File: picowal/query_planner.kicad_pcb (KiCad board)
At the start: 4 copper layers, 100 x 55 mm, 23 parts, among them J1 UP, J2 DN, J3 UART, J4 SWD_QRY, J5 RJ45, J6 SWD_IDX, U1 iCE40HX8K, U10 AP2112K_1V2, U11 RP2354B_IDX, U12 PSRAM_IDX, U13 W5500, U14 W25Q128_IDX, U15 TPS62A01_IDX, U2 RP2354B_QRY, U3 SRAM_A, U4 SRAM_B, U5 PSRAM_QRY, U6 W25Q128_QRY, U7 W25Q32, U8 TPS62A01_QRY, U9 AP2112K_3V3, Y1 12MHz, Y2 25MHz

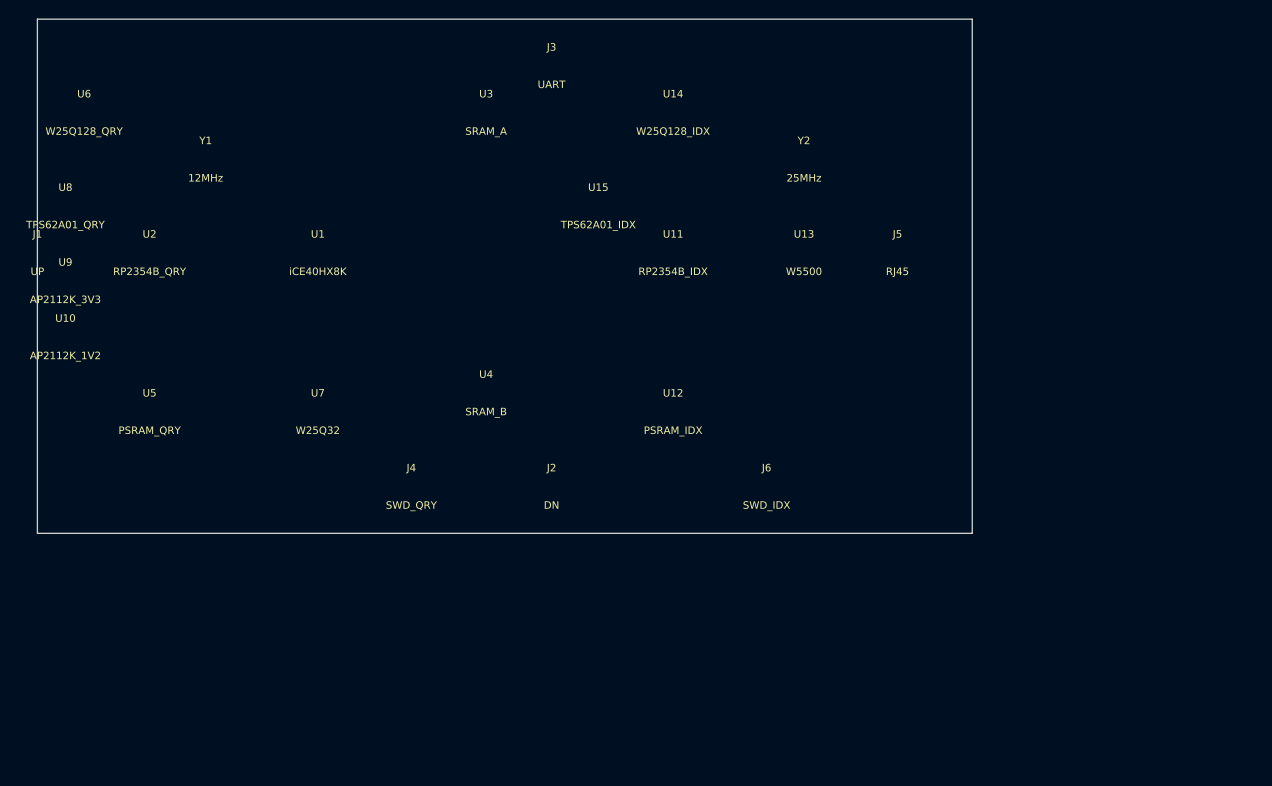
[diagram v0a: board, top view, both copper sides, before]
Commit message: Upgrade PicoWAL: iCE40HX8K → ECP5-5G-45F + 3× NVMe M.2 RAID
Swap FPGA to LFE5UM5G-45F (CABGA381) for 4× 3.125Gbps SerDes.
3 SerDes channels → PCIe Gen1 x1 → M.2 M-key NVMe drives (RAID).
4th SerDes spare for future upstream PCIe or inter-card link.

New components:
  - 3× M.2 M-key NVMe connectors (J7/J8/J9)
  - 100MHz LVDS differential oscillator (PCIe refclk)
  - TPS54331 3A buck for NVMe 3.3V power rail
  - TPS62A02 buck for ECP5 1.1V core (replaces AP2112K-1.2 LDO)
  - W25Q128 replaces W25Q32 for ECP5 config (45F bitstream is larger)

Board: 100×55mm → 130×80mm to accommodate M.2 slots.
BOM: £31.90 → £48.60 (excl. NVMe SSDs).
Pin budget: 110/205 I/O + 3/4 SerDes channels used.
Power: 2.8W board logic + ~10W for 3× NVMe drives.
RTL tests: 15/15 PASS (comment-only changes in query_bypass.v).

Co-authored-by: Copilot <223556219+Copilot@users.noreply.github.com>
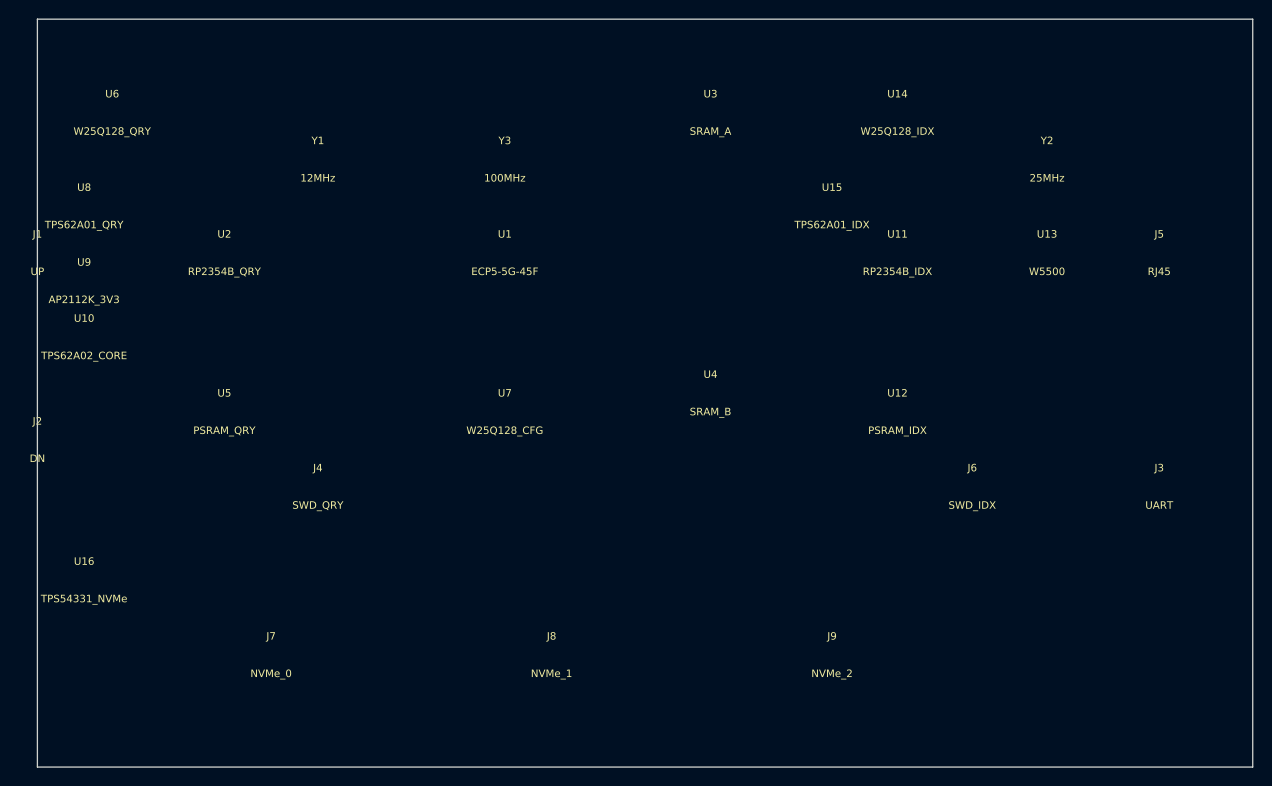
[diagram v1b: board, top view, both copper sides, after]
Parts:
- added J7: NVMe_0, Connector_M2:M2_M_Key_22x80, F.Cu at (25.0, 68.0)
- added J8: NVMe_1, Connector_M2:M2_M_Key_22x80, F.Cu at (55.0, 68.0)
- added J9: NVMe_2, Connector_M2:M2_M_Key_22x80, F.Cu at (85.0, 68.0)
- added U16: TPS54331_NVMe, Package_SO:SOIC-8_3.9x4.9mm_P1.27mm, F.Cu at (5.00, 60.0)
- added Y3: 100MHz, Oscillator:Oscillator_SMD_3225-4Pin_3.2x2.5mm, F.Cu at (50.0, 15.0)
- U1: value iCE40HX8K -> ECP5-5G-45F; footprint Package_BGA:BGA-256_14x14mm_P0.8mm -> Package_BGA:BGA-381_17x17mm_P0.8mm
- U10: value AP2112K_1V2 -> TPS62A02_CORE; footprint Package_TO_SOT_SMD:SOT-23-5 -> Package_TO_SOT_SMD:SOT-23-6
- U7: value W25Q32 -> W25Q128_CFG
- moved J3 79.1 mm to (120.0, 50.0)
- moved J2 55.2 mm to (0.00, 45.0)
- moved J5 28.0 mm to (120.0, 25.0)
- moved U13 26.0 mm to (108.0, 25.0)
- moved Y2 26.0 mm to (108.0, 15.0)
- moved U15 25.0 mm to (85.0, 20.0)
- moved U11 24.0 mm to (92.0, 25.0)
- moved U12 24.0 mm to (92.0, 42.0)
- moved U14 24.0 mm to (92.0, 10.0)
- moved U3 24.0 mm to (72.0, 10.0)
- moved U4 24.0 mm to (72.0, 40.0)
- moved J6 22.0 mm to (100.0, 50.0)
- moved U1 20.0 mm to (50.0, 25.0)
- moved U7 20.0 mm to (50.0, 42.0)
- moved Y1 12.0 mm to (30.0, 15.0)
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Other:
- board size 100 x 55 mm -> 130 x 80 mm
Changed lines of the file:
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@@
   (setup (grid_origin 0 0)
     (pcbplotparams (layerselection 0x00010fc_ffffffff) (outputdirectory "")))
-  (gr_rect (start 0 0) (end 100 55)
+  (gr_rect (start 0 0) (end 130 80)
     (stroke (width 0.1) (type default)) (fill none) (layer "Edge.Cuts"))
-  (footprint "Package_BGA:BGA-256_14x14mm_P0.8mm"
-    (at 30 25) (layer "F.Cu")
+  (footprint "Package_BGA:BGA-381_17x17mm_P0.8mm"
+    (at 50 25) (layer "F.Cu")
     (property "Reference" "U1" (at 0 -2 0) (layer "F.SilkS")
       (effects (font (size 0.8 0.8) (thickness 0.12))))
-    (property "Value" "iCE40HX8K" (at 0 2 0) (layer "F.SilkS")
+    (property "Value" "ECP5-5G-45F" (at 0 2 0) (layer "F.SilkS")
       (effects (font (size 0.8 0.8) (thickness 0.12)))))
   (footprint "Package_DFN_QFN:QFN-80-1EP_10x10mm_P0.4mm_EP5.45x5.45mm"
-    (at 12 25) (layer "F.Cu")
+    (at 20 25) (layer "F.Cu")
     (property "Reference" "U2" (at 0 -2 0) (layer "F.SilkS")
       (effects (font (size 0.8 0.8) (thickness 0.12))))
@@
       (effects (font (size 0.8 0.8) (thickness 0.12)))))
   (footprint "Package_SO:TSOP-II-44_10.16x18.41mm_P0.8mm"
-    (at 48 10) (layer "F.Cu")
+    (at 72 10) (layer "F.Cu")
     (property "Reference" "U3" (at 0 -2 0) (layer "F.SilkS")
       (effects (font (size 0.8 0.8) (thickness 0.12))))
@@
       (effects (font (size 0.8 0.8) (thickness 0.12)))))
   (footprint "Package_SO:TSOP-II-44_10.16x18.41mm_P0.8mm"
-    (at 48 40) (layer "F.Cu")
+    (at 72 40) (layer "F.Cu")
     (property "Reference" "U4" (at 0 -2 0) (layer "F.SilkS")
       (effects (font (size 0.8 0.8) (thickness 0.12))))
@@
       (effects (font (size 0.8 0.8) (thickness 0.12)))))
   (footprint "Package_SO:SOP-8_3.9x4.9mm_P1.27mm"
-    (at 12 42) (layer "F.Cu")
+    (at 20 42) (layer "F.Cu")
     (property "Reference" "U5" (at 0 -2 0) (layer "F.SilkS")
       (effects (font (size 0.8 0.8) (thickness 0.12))))
@@
       (effects (font (size 0.8 0.8) (thickness 0.12)))))
   (footprint "Package_SO:SOIC-8_3.9x4.9mm_P1.27mm"
-    (at 5 10) (layer "F.Cu")
+    (at 8 10) (layer "F.Cu")
     (property "Reference" "U6" (at 0 -2 0) (layer "F.SilkS")
       (effects (font (size 0.8 0.8) (thickness 0.12))))
@@
       (effects (font (size 0.8 0.8) (thickness 0.12)))))
   (footprint "Package_SO:SOIC-8_3.9x4.9mm_P1.27mm"
-    (at 30 42) (layer "F.Cu")
+    (at 50 42) (layer "F.Cu")
     (property "Reference" "U7" (at 0 -2 0) (layer "F.SilkS")
       (effects (font (size 0.8 0.8) (thickness 0.12))))
-    (property "Value" "W25Q32" (at 0 2 0) (layer "F.SilkS")
+    (property "Value" "W25Q128_CFG" (at 0 2 0) (layer "F.SilkS")
       (effects (font (size 0.8 0.8) (thickness 0.12)))))
   (footprint "Package_TO_SOT_SMD:SOT-23-6"
-    (at 3 20) (layer "F.Cu")
+    (at 5 20) (layer "F.Cu")
     (property "Reference" "U8" (at 0 -2 0) (layer "F.SilkS")
       (effects (font (size 0.8 0.8) (thickness 0.12))))
@@
       (effects (font (size 0.8 0.8) (thickness 0.12)))))
   (footprint "Package_TO_SOT_SMD:SOT-23-5"
-    (at 3 28) (layer "F.Cu")
+    (at 5 28) (layer "F.Cu")
     (property "Reference" "U9" (at 0 -2 0) (layer "F.SilkS")
       (effects (font (size 0.8 0.8) (thickness 0.12))))
     (property "Value" "AP2112K_3V3" (at 0 2 0) (layer "F.SilkS")
       (effects (font (size 0.8 0.8) (thickness 0.12)))))
-  (footprint "Package_TO_SOT_SMD:SOT-23-5"
-    (at 3 34) (layer "F.Cu")
+  (footprint "Package_TO_SOT_SMD:SOT-23-6"
+    (at 5 34) (layer "F.Cu")
     (property "Reference" "U10" (at 0 -2 0) (layer "F.SilkS")
       (effects (font (size 0.8 0.8) (thickness 0.12))))
-    (property "Value" "AP2112K_1V2" (at 0 2 0) (layer "F.SilkS")
+    (property "Value" "TPS62A02_CORE" (at 0 2 0) (layer "F.SilkS")
       (effects (font (size 0.8 0.8) (thickness 0.12)))))
   (footprint "Package_DFN_QFN:QFN-80-1EP_10x10mm_P0.4mm_EP5.45x5.45mm"
-    (at 68 25) (layer "F.Cu")
+    (at 92 25) (layer "F.Cu")
     (property "Reference" "U11" (at 0 -2 0) (layer "F.SilkS")
       (effects (font (size 0.8 0.8) (thickness 0.12))))
@@
       (effects (font (size 0.8 0.8) (thickness 0.12)))))
   (footprint "Package_SO:SOP-8_3.9x4.9mm_P1.27mm"
-    (at 68 42) (layer "F.Cu")
+    (at 92 42) (layer "F.Cu")
     (property "Reference" "U12" (at 0 -2 0) (layer "F.SilkS")
       (effects (font (size 0.8 0.8) (thickness 0.12))))
@@
       (effects (font (size 0.8 0.8) (thickness 0.12)))))
   (footprint "Package_QFP:LQFP-48_7x7mm_P0.5mm"
-    (at 82 25) (layer "F.Cu")
+    (at 108 25) (layer "F.Cu")
     (property "Reference" "U13" (at 0 -2 0) (layer "F.SilkS")
       (effects (font (size 0.8 0.8) (thickness 0.12))))
@@
       (effects (font (size 0.8 0.8) (thickness 0.12)))))
   (footprint "Package_SO:SOIC-8_3.9x4.9mm_P1.27mm"
-    (at 68 10) (layer "F.Cu")
+    (at 92 10) (layer "F.Cu")
     (property "Reference" "U14" (at 0 -2 0) (layer "F.SilkS")
       (effects (font (size 0.8 0.8) (thickness 0.12))))
@@
       (effects (font (size 0.8 0.8) (thickness 0.12)))))
   (footprint "Package_TO_SOT_SMD:SOT-23-6"
-    (at 60 20) (layer "F.Cu")
+    (at 85 20) (layer "F.Cu")
     (property "Reference" "U15" (at 0 -2 0) (layer "F.SilkS")
       (effects (font (size 0.8 0.8) (thickness 0.12))))
     (property "Value" "TPS62A01_IDX" (at 0 2 0) (layer "F.SilkS")
       (effects (font (size 0.8 0.8) (thickness 0.12)))))
+  (footprint "Package_SO:SOIC-8_3.9x4.9mm_P1.27mm"
+    (at 5 60) (layer "F.Cu")
+    (property "Reference" "U16" (at 0 -2 0) (layer "F.SilkS")
+      (effects (font (size 0.8 0.8) (thickness 0.12))))
+    (property "Value" "TPS54331_NVMe" (at 0 2 0) (layer "F.SilkS")
+      (effects (font (size 0.8 0.8) (thickness 0.12)))))
+  (footprint "Connector_M2:M2_M_Key_22x80"
+    (at 25 68) (layer "F.Cu")
+    (property "Reference" "J7" (at 0 -2 0) (layer "F.SilkS")
+      (effects (font (size 0.8 0.8) (thickness 0.12))))
+    (property "Value" "NVMe_0" (at 0 2 0) (layer "F.SilkS")
+      (effects (font (size 0.8 0.8) (thickness 0.12)))))
+  (footprint "Connector_M2:M2_M_Key_22x80"
+    (at 55 68) (layer "F.Cu")
+    (property "Reference" "J8" (at 0 -2 0) (layer "F.SilkS")
+      (effects (font (size 0.8 0.8) (thickness 0.12))))
+    (property "Value" "NVMe_1" (at 0 2 0) (layer "F.SilkS")
+      (effects (font (size 0.8 0.8) (thickness 0.12)))))
+  (footprint "Connector_M2:M2_M_Key_22x80"
+    (at 85 68) (layer "F.Cu")
+    (property "Reference" "J9" (at 0 -2 0) (layer "F.SilkS")
+      (effects (font (size 0.8 0.8) (thickness 0.12))))
+    (property "Value" "NVMe_2" (at 0 2 0) (layer "F.SilkS")
+      (effects (font (size 0.8 0.8) (thickness 0.12)))))
   (footprint "Crystal:Crystal_SMD_3215-2Pin_3.2x1.5mm"
-    (at 18 15) (layer "F.Cu")
+    (at 30 15) (layer "F.Cu")
     (property "Reference" "Y1" (at 0 -2 0) (layer "F.SilkS")
       (effects (font (size 0.8 0.8) (thickness 0.12))))
@@
       (effects (font (size 0.8 0.8) (thickness 0.12)))))
   (footprint "Crystal:Crystal_SMD_3215-2Pin_3.2x1.5mm"
-    (at 82 15) (layer "F.Cu")
+    (at 108 15) (layer "F.Cu")
     (property "Reference" "Y2" (at 0 -2 0) (layer "F.SilkS")
       (effects (font (size 0.8 0.8) (thickness 0.12))))
     (property "Value" "25MHz" (at 0 2 0) (layer "F.SilkS")
+      (effects (font (size 0.8 0.8) (thickness 0.12)))))
+  (footprint "Oscillator:Oscillator_SMD_3225-4Pin_3.2x2.5mm"
+    (at 50 15) (layer "F.Cu")
+    (property "Reference" "Y3" (at 0 -2 0) (layer "F.SilkS")
+      (effects (font (size 0.8 0.8) (thickness 0.12))))
+    (property "Value" "100MHz" (at 0 2 0) (layer "F.SilkS")
       (effects (font (size 0.8 0.8) (thickness 0.12)))))
   (footprint "Connector_PinHeader_2.54mm:PinHeader_2x10_P2.54mm_Vertical"
@@
       (effects (font (size 0.8 0.8) (thickness 0.12)))))
   (footprint "Connector_PinHeader_2.54mm:PinHeader_2x10_P2.54mm_Vertical"
-    (at 55 50) (layer "F.Cu")
+    (at 0 45) (layer "F.Cu")
     (property "Reference" "J2" (at 0 -2 0) (layer "F.SilkS")
       (effects (font (size 0.8 0.8) (thickness 0.12))))
@@
       (effects (font (size 0.8 0.8) (thickness 0.12)))))
   (footprint "Connector_PinHeader_2.54mm:PinHeader_1x04_P2.54mm_Vertical"
-    (at 55 5) (layer "F.Cu")
+    (at 120 50) (layer "F.Cu")
     (property "Reference" "J3" (at 0 -2 0) (layer "F.SilkS")
       (effects (font (size 0.8 0.8) (thickness 0.12))))
@@
       (effects (font (size 0.8 0.8) (thickness 0.12)))))
   (footprint "Connector_PinHeader_1.27mm:PinHeader_1x05_P1.27mm_Vertical"
-    (at 40 50) (layer "F.Cu")
+    (at 30 50) (layer "F.Cu")
     (property "Reference" "J4" (at 0 -2 0) (layer "F.SilkS")
       (effects (font (size 0.8 0.8) (thickness 0.12))))
@@
       (effects (font (size 0.8 0.8) (thickness 0.12)))))
   (footprint "Connector_RJ45:RJ45_Amphenol_ARJM11C7"
-    (at 92 25) (layer "F.Cu")
+    (at 120 25) (layer "F.Cu")
     (property "Reference" "J5" (at 0 -2 0) (layer "F.SilkS")
       (effects (font (size 0.8 0.8) (thickness 0.12))))
@@
       (effects (font (size 0.8 0.8) (thickness 0.12)))))
   (footprint "Connector_PinHeader_1.27mm:PinHeader_1x05_P1.27mm_Vertical"
-    (at 78 50) (layer "F.Cu")
+    (at 100 50) (layer "F.Cu")
     (property "Reference" "J6" (at 0 -2 0) (layer "F.SilkS")
       (effects (font (size 0.8 0.8) (thickness 0.12))))

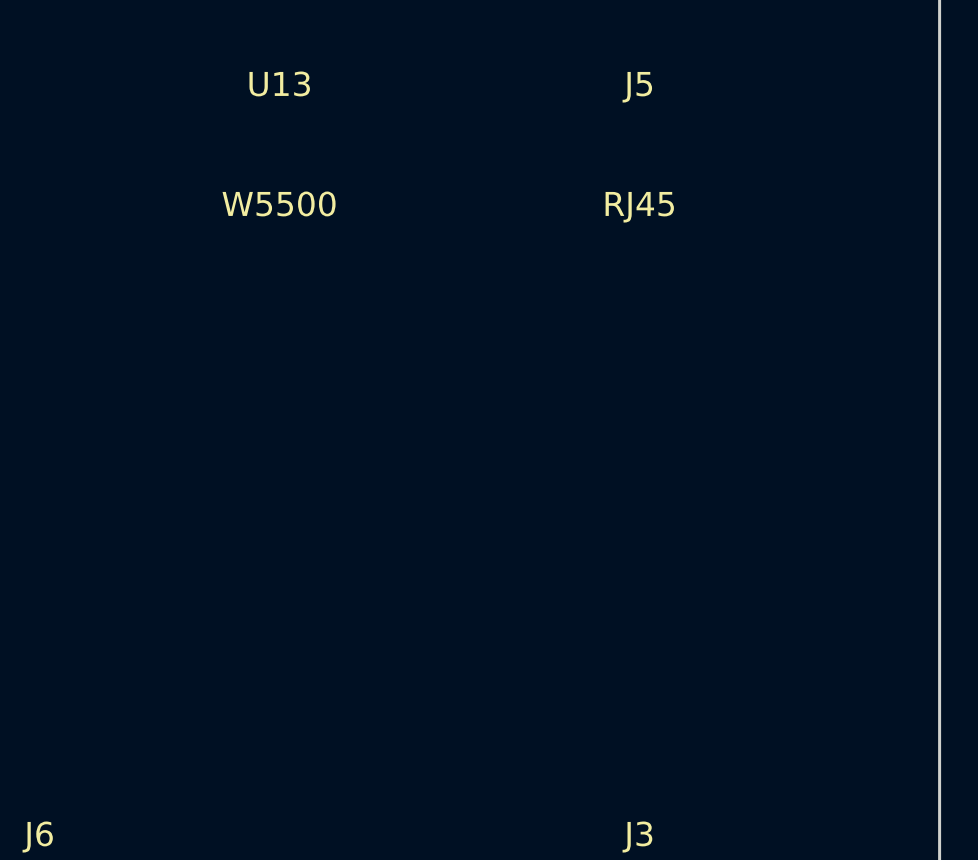
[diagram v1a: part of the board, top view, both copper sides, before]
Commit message: Add deterministic 8-bit parallel bus, swap SPI for pico interfaces
- New RTL: fpga_pico_bus.v — 8-bit bidirectional bus with RDY/ACK handshake
  - DATA[7:0] + RDY + ACK + DIR + SOF + EOF + SOCK[1:0] = 15 pins/pico
  - TX FIFO (512 bytes), ACK synchronizer (3-stage CDC)
  - Timeout recovery, direction turnaround dead cycle
  - ~50 MB/s @ 50MHz, PIO+DMA friendly on pico side

- Deterministic architecture:
  - Pico A (QRY): owns TCP streams, parses queries, streams results
  - Pico B (IDX): owns all writes, WAL, index maintenance (no contention)
  - Direct reads: FPGA -> NVMe -> TCP (zero pico, deterministic pipeline)
  - Drive 0,1 = data shards, Drive 2 = WAL + indexes (pico B exclusive)

- Generator updated: SPI register map -> 8-bit parallel bus pins
  - Pin budget: 133/205 (was 114/205 with SPI — +19 pins, still comfortable)
  - ECP5 symbol updated with QRY_D[0:7]/IDX_D[0:7] bus pins

- Testbench: tb_fpga_pico_bus.v — 12/12 PASS
  - TX single/multi-byte, timeout, RX, bidirectional, FIFO backpressure, reset

Co-authored-by: Copilot <223556219+Copilot@users.noreply.github.com>
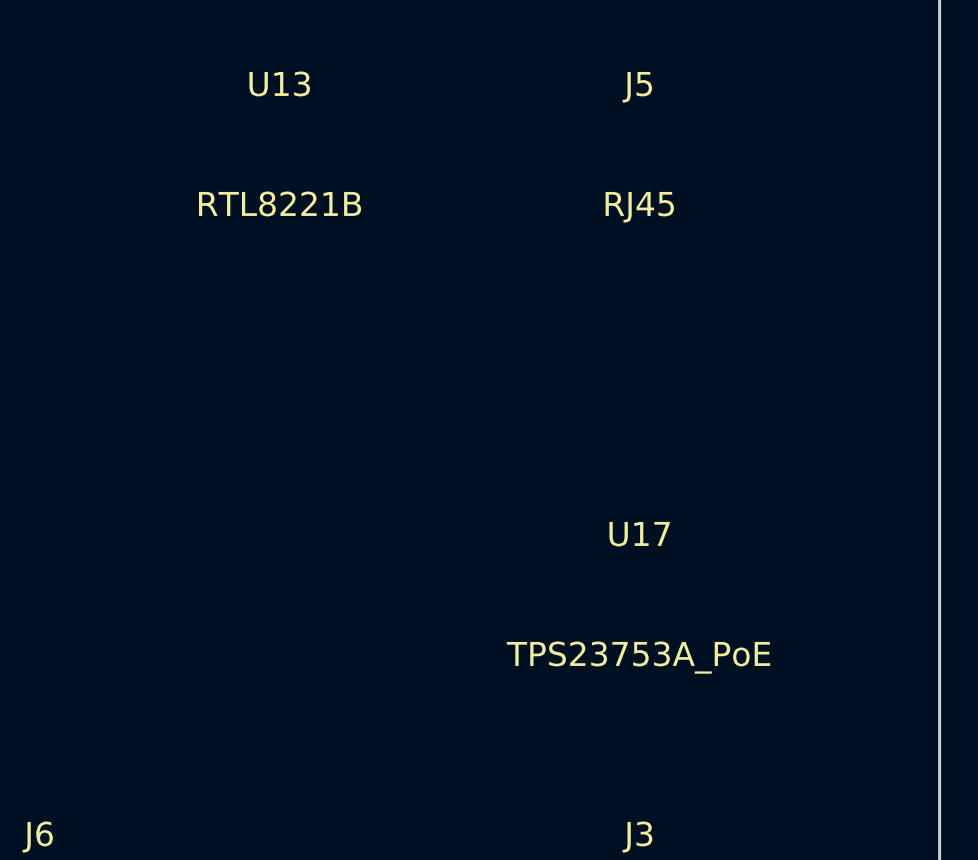
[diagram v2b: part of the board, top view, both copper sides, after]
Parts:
- added U17: TPS23753A_PoE, Package_SO:TSSOP-20_4.4x6.5mm_P0.65mm, F.Cu at (120.0, 40.0)
- U13: value W5500 -> RTL8221B; footprint Package_QFP:LQFP-48_7x7mm_P0.5mm -> Package_DFN_QFN:QFN-56_7x7mm_P0.4mm
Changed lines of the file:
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@@
     (property "Value" "PSRAM_IDX" (at 0 2 0) (layer "F.SilkS")
       (effects (font (size 0.8 0.8) (thickness 0.12)))))
-  (footprint "Package_QFP:LQFP-48_7x7mm_P0.5mm"
+  (footprint "Package_DFN_QFN:QFN-56_7x7mm_P0.4mm"
     (at 108 25) (layer "F.Cu")
     (property "Reference" "U13" (at 0 -2 0) (layer "F.SilkS")
       (effects (font (size 0.8 0.8) (thickness 0.12))))
-    (property "Value" "W5500" (at 0 2 0) (layer "F.SilkS")
+    (property "Value" "RTL8221B" (at 0 2 0) (layer "F.SilkS")
       (effects (font (size 0.8 0.8) (thickness 0.12)))))
   (footprint "Package_SO:SOIC-8_3.9x4.9mm_P1.27mm"
@@
     (property "Value" "TPS54331_NVMe" (at 0 2 0) (layer "F.SilkS")
       (effects (font (size 0.8 0.8) (thickness 0.12)))))
+  (footprint "Package_SO:TSSOP-20_4.4x6.5mm_P0.65mm"
+    (at 120 40) (layer "F.Cu")
+    (property "Reference" "U17" (at 0 -2 0) (layer "F.SilkS")
+      (effects (font (size 0.8 0.8) (thickness 0.12))))
+    (property "Value" "TPS23753A_PoE" (at 0 2 0) (layer "F.SilkS")
+      (effects (font (size 0.8 0.8) (thickness 0.12)))))
   (footprint "Connector_M2:M2_M_Key_22x80"
